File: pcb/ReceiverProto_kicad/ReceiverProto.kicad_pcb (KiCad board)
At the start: 4 copper layers, 75 x 50 mm, 65 parts, among them J1 Conn_01x09, J2 Conn_01x03, J3 Conn_01x04, J4 Conn_01x06, U11 ADM8660ARZ-REEL, U12 ADP7182AUJZ-1.8-R7, U13 ADA4807-1, U14 ADA4807-1, U15 ADA4807-1, U16 ADA4807-1, U4 AD7387BCPZ-RL7, U5 TLV9001IDCK, U6 TLV9001IDCK, U7 TPS79301DBVR

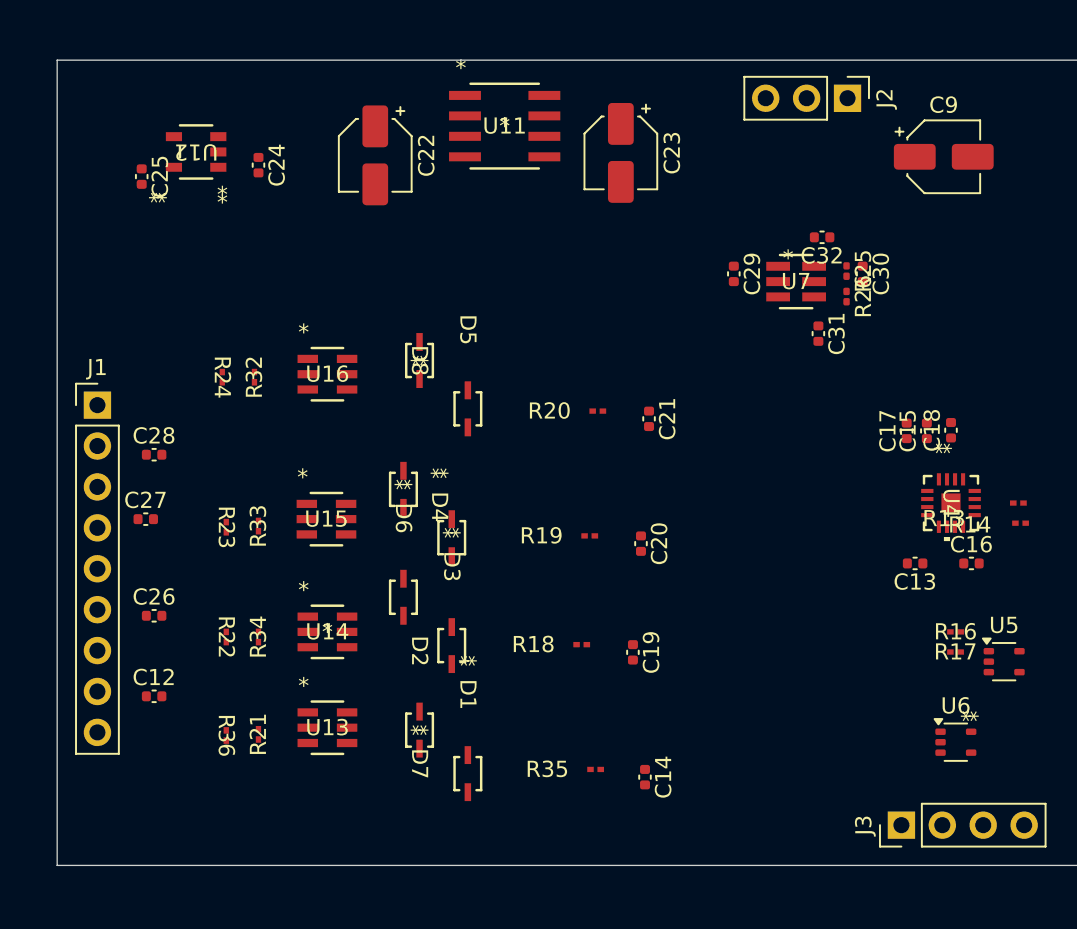
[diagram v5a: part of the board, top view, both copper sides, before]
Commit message: About 60% of the layout for the drivers has been completed, majority of layout still needs to be completed.
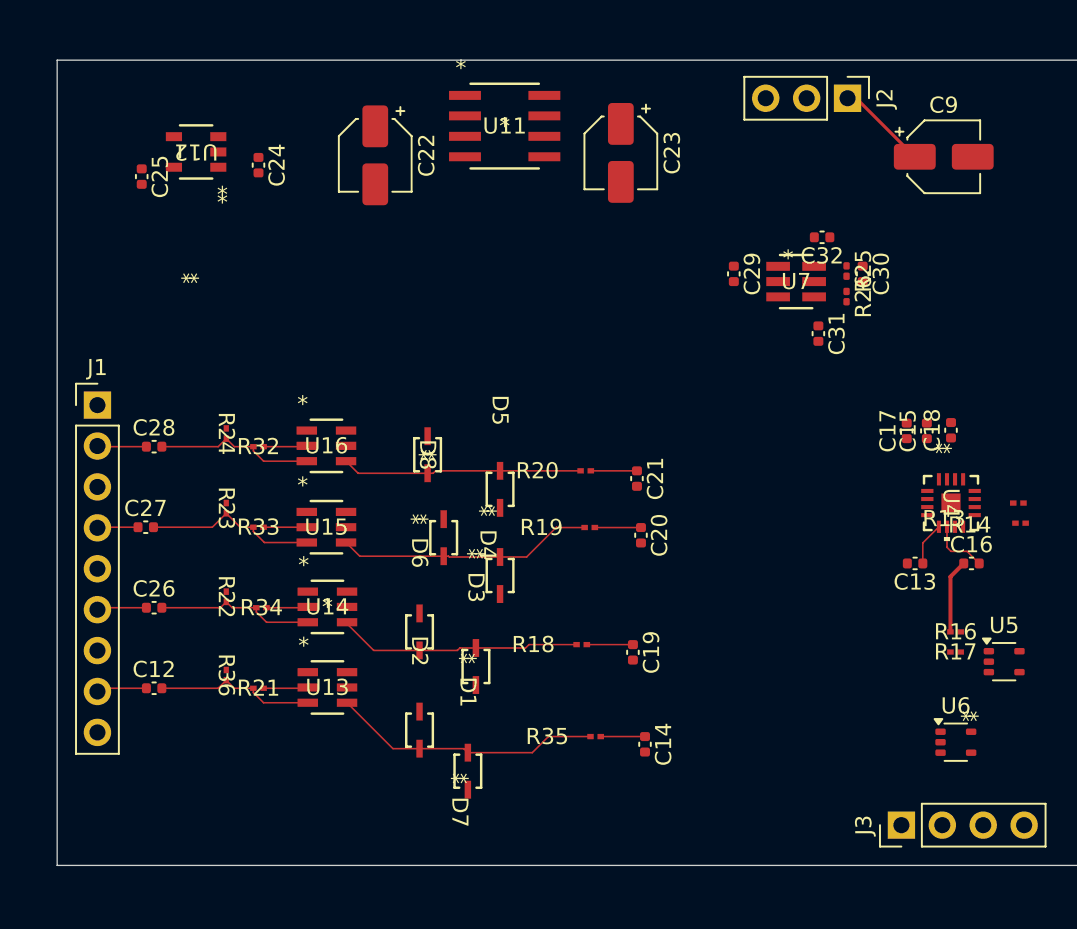
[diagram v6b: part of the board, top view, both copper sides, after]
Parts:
- moved D8 5.87 mm to (128.5, 114.0)
- moved D5 5.39 mm to (133.0, 116.2)
- moved U16 4.45 mm to (122.2, 113.5)
- moved R32 4.32 mm to (118.0, 113.5), turned to 0 degrees
- moved D7 3.91 mm to (129.5, 119.2)
- moved D4 3.81 mm to (133.0, 121.5)
- moved C21 3.79 mm to (141.5, 115.5)
- moved R20 3.79 mm to (138.3, 115.0)
- moved R36 3.75 mm to (116.0, 127.7)
- moved R24 3.51 mm to (116.0, 112.7)
- moved R21 2.87 mm to (118.0, 128.5), turned to 0 degrees
- moved R22 2.50 mm to (116.0, 122.8)
- moved U13 2.50 mm to (122.3, 128.5)
- moved D6 2.37 mm to (128.0, 125.0)
- moved C14 2.04 mm to (142.0, 132.0)
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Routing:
- net Net-(D1-K): track 0.00 -> 16.8 mm
- net Net-(D4-K): track 0.00 -> 16.0 mm
- net Net-(D3-K): track 0.00 -> 15.2 mm
- net Net-(D5-K): track 0.00 -> 14.9 mm
- net Net-(U15-+): track 0.00 -> 10.8 mm
- net -2V5: track 0.00 -> 10.7 mm
- net Net-(U13-+): track 0.00 -> 10.0 mm
- net Net-(U16-+): track 0.00 -> 9.94 mm
- net Net-(U14-+): track 0.00 -> 9.89 mm
- net +5V: track 0.00 -> 5.68 mm
- net /adc/ADC_REFIO: track 0.00 -> 4.59 mm
- net ADC_B1: track 0.00 -> 3.82 mm
- net 0: track 0.00 -> 3.69 mm
- net ADC_B0: track 0.00 -> 3.30 mm
- net ADC_A0: track 0.00 -> 3.12 mm
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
